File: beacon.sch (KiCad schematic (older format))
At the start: 34 parts

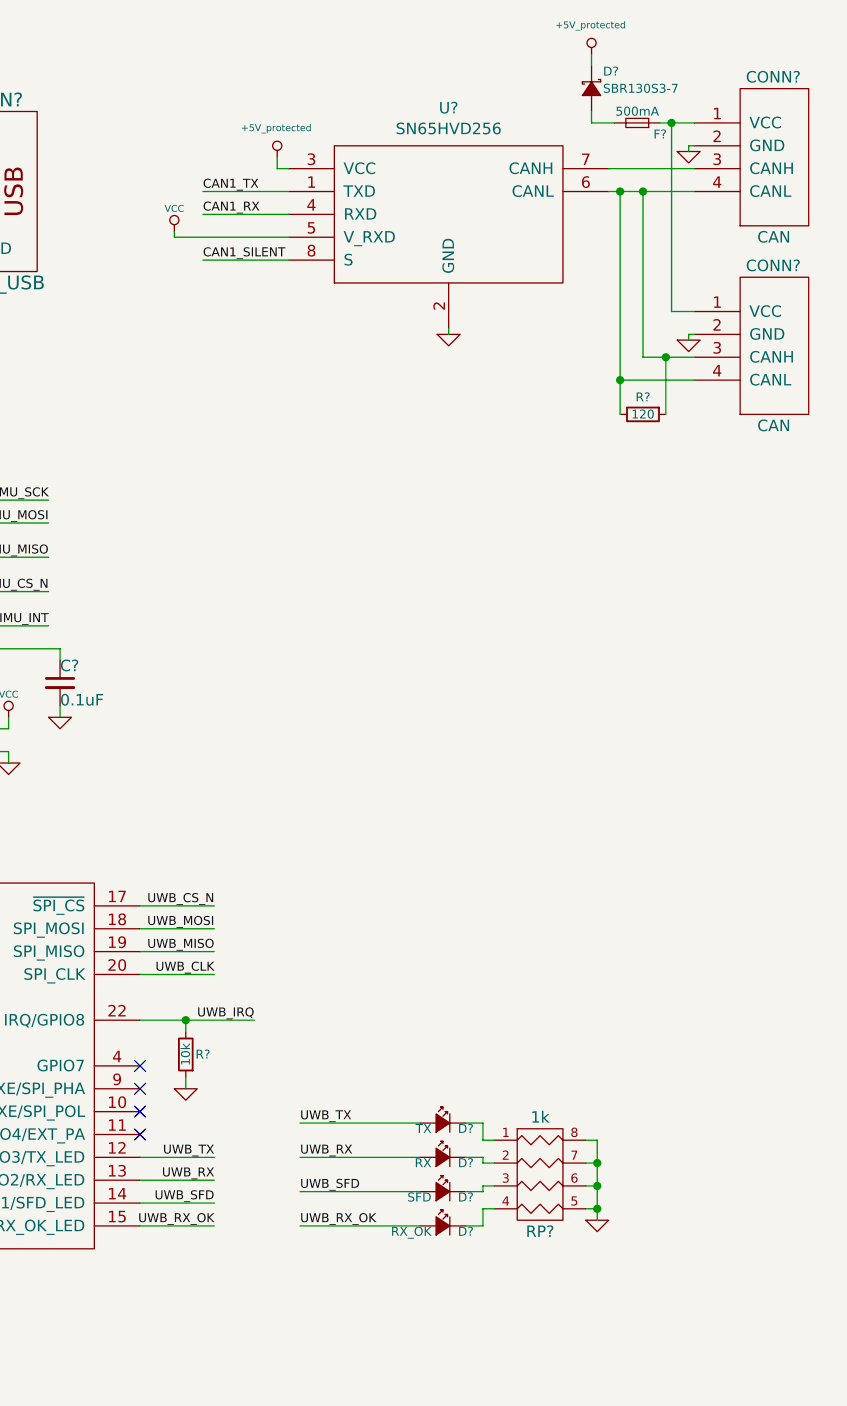
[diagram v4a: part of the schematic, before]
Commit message: Add power regulator for VCC 3.3V
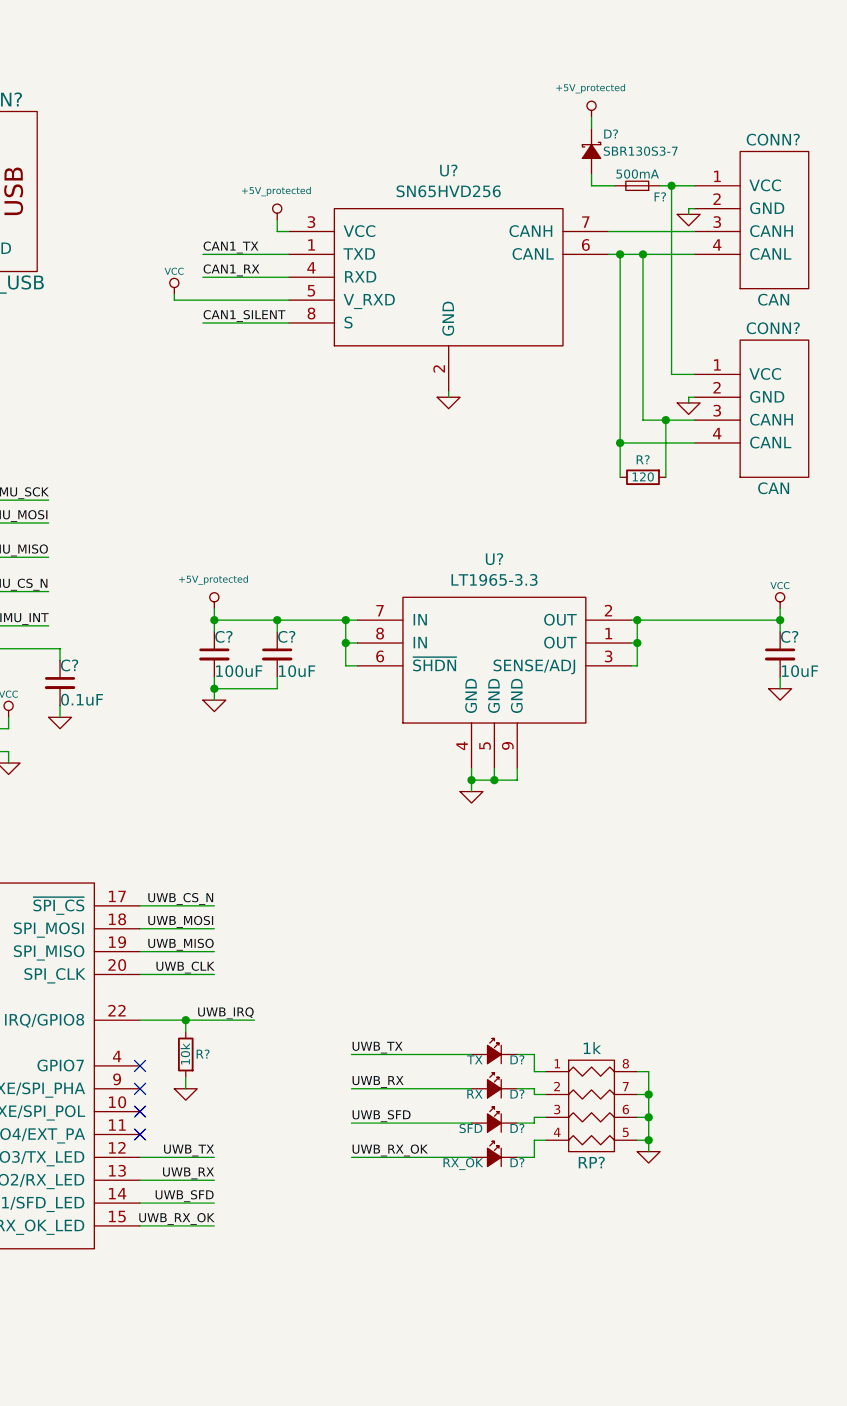
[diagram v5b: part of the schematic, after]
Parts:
- added C? (x2): 10uF, symbol C_Small
- added C?: 100uF, symbol C_Small
- added U?: LT1965-3.3, MODULE, symbol LT1965
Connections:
- net +5V_protected: now also C?.1, C?.1, U?.6 (~SHDN), U?.7 (IN), U?.8 (IN)
- net GND: now also C?.2, C?.2, C?.2, U?.4 (GND), U?.5 (GND), U?.9 (GND)
- net VCC: now also C?.1, U?.1 (OUT), U?.2 (OUT), U?.3 (SENSE/ADJ)
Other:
- moved on the sheet: CONN?, D?, F?, R?, RP?, U?

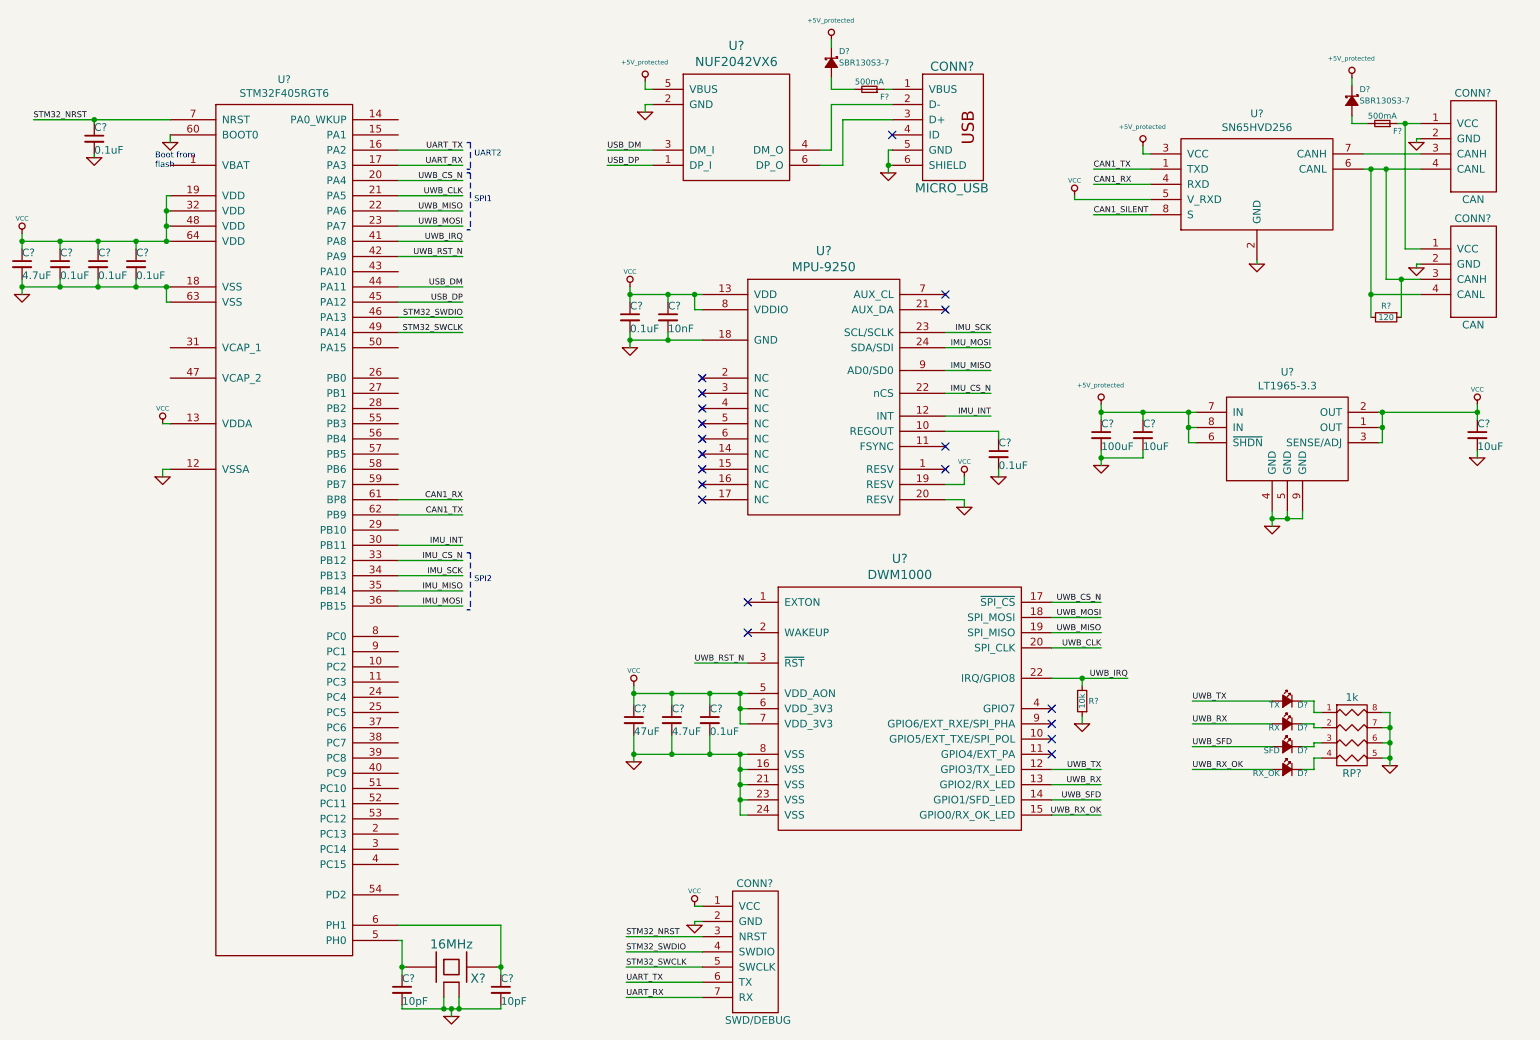
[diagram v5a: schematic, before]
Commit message: Choose an appropriate PTC resettable fuse
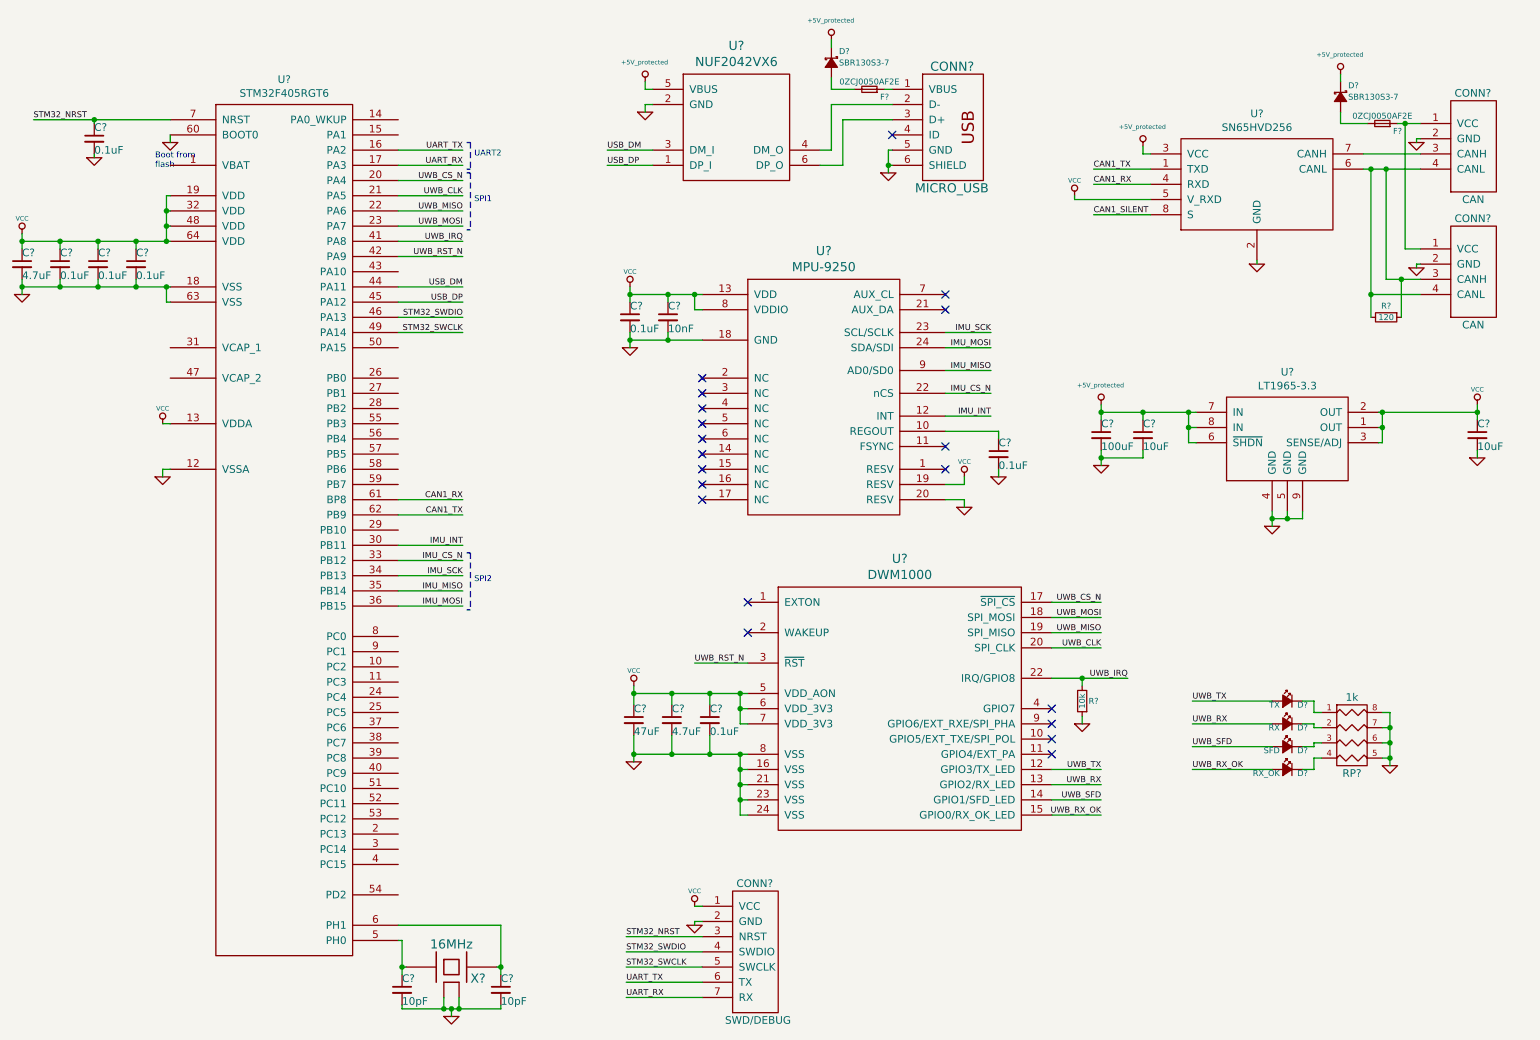
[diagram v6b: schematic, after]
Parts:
- F? (x2): value 500mA -> 0ZCJ0050AF2E
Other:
- moved on the sheet: D?
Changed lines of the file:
@@
 encoding utf-8
 Sheet 1 1
-Title ""
-Date ""
-Rev ""
-Comp ""
+Title "Beacon board"
+Date "2016-06-23"
+Rev "A"
+Comp "CVRA (Club Vaudois de Robotique Autonome)"
 Comment1 ""
 Comment2 ""
@@
 NoConn ~ 7825 5600
 Wire Wire Line
-	1125 1425 2025 1425
+	1125 1425 1525 1425
+Wire Wire Line
+	1525 1425 2025 1425
 Wire Wire Line
 	1525 1425 1525 1450
@@
 Connection ~ 1525 1425
 Wire Wire Line
-	1050 2525 2025 2525
+	1050 2525 1300 2525
+Wire Wire Line
+	1300 2525 1550 2525
+Wire Wire Line
+	1550 2525 1800 2525
+Wire Wire Line
+	1800 2525 2000 2525
+Wire Wire Line
+	2000 2525 2025 2525
 Wire Wire Line
 	2025 2025 2000 2025
 Wire Wire Line
-	2000 2225 2000 1925
+	2000 2225 2000 2125
+Wire Wire Line
+	2000 2125 2000 2025
+Wire Wire Line
+	2000 2025 2000 1925
 Wire Wire Line
 	1975 3425 2025 3425
@@
 	3525 6725 4200 6725
 Wire Wire Line
-	4200 6725 4200 7050
+	4200 6725 4200 7000
+Wire Wire Line
+	4200 7000 4200 7050
 Wire Wire Line
 	4200 7000 4175 7000
 Wire Wire Line
-	3550 6825 3550 7050
+	3550 6825 3550 7000
+Wire Wire Line
+	3550 7000 3550 7050
 Wire Wire Line
 	3550 7000 3575 7000
@@
 	3875 7275 3875 7325
 Wire Wire Line
-	3550 7275 4200 7275
+	3550 7275 3825 7275
+Wire Wire Line
+	3825 7275 3875 7275
+Wire Wire Line
+	3875 7275 3925 7275
+Wire Wire Line
+	3925 7275 4200 7275
 Wire Wire Line
 	3825 7275 3825 7200
@@
 	3525 2525 3950 2525
 Wire Wire Line
-	1050 2225 2025 2225
+	1050 2225 1300 2225
+Wire Wire Line
+	1300 2225 1550 2225
+Wire Wire Line
+	1550 2225 1800 2225
+Wire Wire Line
+	1800 2225 2000 2225
+Wire Wire Line
+	2000 2225 2025 2225
 Wire Wire Line
 	1800 2225 1800 2275
@@
 Connection ~ 1550 2525
 Wire Wire Line
-	1050 2475 1050 2575
+	1050 2475 1050 2525
+Wire Wire Line
+	1050 2525 1050 2575
 Connection ~ 1300 2525
 Connection ~ 1050 2525
@@
 	2000 1925 2025 1925
 Wire Wire Line
-	1050 2175 1050 2275
+	1050 2175 1050 2225
+Wire Wire Line
+	1050 2225 1050 2275
 Wire Wire Line
 	1550 2275 1550 2225
@@
 	5775 5400 5825 5400
 Wire Wire Line
-	5775 5200 5775 5400
+	5775 5200 5775 5300
+Wire Wire Line
+	5775 5300 5775 5400
 Wire Wire Line
 	5575 5200 5575 5275
@@
 Connection ~ 5575 5200
 Wire Wire Line
-	5075 5150 5075 5275
+	5075 5150 5075 5200
+Wire Wire Line
+	5075 5200 5075 5275
 Connection ~ 5325 5200
 Wire Wire Line
@@
 Connection ~ 5775 5300
 Wire Wire Line
-	5075 5600 5825 5600
-Wire Wire Line
-	5775 5600 5775 6000
+	5075 5600 5325 5600
+Wire Wire Line
+	5325 5600 5575 5600
+Wire Wire Line
+	5575 5600 5775 5600
+Wire Wire Line
+	5775 5600 5825 5600
+Wire Wire Line
+	5775 5600 5775 5700
+Wire Wire Line
+	5775 5700 5775 5800
+Wire Wire Line
+	5775 5800 5775 5900
+Wire Wire Line
+	5775 5900 5775 6000
 Wire Wire Line
 	5775 5700 5825 5700
@@
 Connection ~ 5575 5600
 Wire Wire Line
-	5075 5475 5075 5650
+	5075 5475 5075 5600
+Wire Wire Line
+	5075 5600 5075 5650
 Connection ~ 5325 5600
 Connection ~ 5775 5200
 Wire Wire Line
-	5075 5200 5825 5200
+	5075 5200 5325 5200
+Wire Wire Line
+	5325 5200 5575 5200
+Wire Wire Line
+	5575 5200 5775 5200
+Wire Wire Line
+	5775 5200 5825 5200
 Connection ~ 5075 5600
 Connection ~ 5075 5200
@@
 	7825 4900 8150 4900
 Wire Wire Line
-	7825 5100 8325 5100
+	7825 5100 8025 5100
+Wire Wire Line
+	8025 5100 8325 5100
 Wire Wire Line
 	8025 5150 8025 5100
@@
 $EndComp
 Wire Wire Line
-	10050 5325 10050 5675
+	10050 5325 10050 5425
+Wire Wire Line
+	10050 5425 10050 5525
+Wire Wire Line
+	10050 5525 10050 5625
+Wire Wire Line
+	10050 5625 10050 5675
 Wire Wire Line
 	10050 5625 10000 5625
@@
 $EndComp
 Wire Wire Line
-	6750 1625 6750 1775
+	6750 1625 6750 1725
+Wire Wire Line
+	6750 1725 6750 1775
 Wire Wire Line
 	6750 1725 6775 1725
@@
 P 6625 1225
 F 0 "F?" H 6525 1275 39  0000 C CNN
-F 1 "500mA" H 6625 1175 39  0000 C CNN
+F 1 "0ZCJ0050AF2E" H 6625 1175 39  0000 C CNN
 F 2 "" H 6625 1225 50  0000 C CNN
 F 3 "" H 6625 1225 50  0000 C CNN
@@
 	5475 2575 5475 2675
 Wire Wire Line
-	5050 2575 5525 2575
+	5050 2575 5300 2575
+Wire Wire Line
+	5300 2575 5475 2575
+Wire Wire Line
+	5475 2575 5525 2575
 Wire Wire Line
 	5475 2675 5525 2675
@@
 $EndComp
 Wire Wire Line
-	5050 2875 5525 2875
+	5050 2875 5300 2875
+Wire Wire Line
+	5300 2875 5525 2875
 Wire Wire Line
 	5300 2875 5300 2825
 Wire Wire Line
-	5050 2825 5050 2925
+	5050 2825 5050 2875
+Wire Wire Line
+	5050 2875 5050 2925
 Connection ~ 5300 2875
 Wire Wire Line
 	5300 2625 5300 2575
 Wire Wire Line
-	5050 2525 5050 2625
+	5050 2525 5050 2575
+Wire Wire Line
+	5050 2575 5050 2625
 Connection ~ 5300 2575
 Connection ~ 5050 2575
@@
 	9875 1650 10250 1650
 Wire Wire Line
-	9875 1750 10250 1750
-Wire Wire Line
-	9925 1750 9925 2725
+	9875 1750 9925 1750
+Wire Wire Line
+	9925 1750 10025 1750
+Wire Wire Line
+	10025 1750 10250 1750
+Wire Wire Line
+	9925 1750 9925 2575
+Wire Wire Line
+	9925 2575 9925 2725
 Wire Wire Line
 	9925 2575 10250 2575
 Connection ~ 9925 1750
 Wire Wire Line
-	10025 2475 10250 2475
+	10025 2475 10125 2475
+Wire Wire Line
+	10125 2475 10250 2475
 Wire Wire Line
 	10025 2475 10025 1750
@@
 P 10000 1450
 F 0 "F?" H 9900 1500 39  0000 C CNN
-F 1 "500mA" H 10000 1400 39  0000 C CNN
+F 1 "0ZCJ0050AF2E" H 10000 1400 39  0000 C CNN
 F 2 "" H 10000 1450 50  0000 C CNN
 F 3 "" H 10000 1450 50  0000 C CNN
@@
 	10225 1550 10225 1575
 Wire Wire Line
-	10100 1450 10250 1450
+	10100 1450 10150 1450
+Wire Wire Line
+	10150 1450 10250 1450
 Wire Wire Line
 	10150 2275 10150 1450
@@
 L D_Schottky_Small D?
 U 1 1 576C666F
-P 9800 1300
-F 0 "D?" V 9725 1350 39  0000 L CNN
-F 1 "SBR130S3-7" V 9800 1350 39  0000 L CNN
-F 2 "" V 9800 1300 50  0000 C CNN
-F 3 "" V 9800 1300 50  0000 C CNN
-	1    9800 1300
+P 9725 1275
+F 0 "D?" V 9650 1325 39  0000 L CNN
+F 1 "SBR130S3-7" V 9725 1325 39  0000 L CNN
+F 2 "" V 9725 1275 50  0000 C CNN
+F 3 "" V 9725 1275 50  0000 C CNN
+	1    9725 1275
 	0    1    1    0
 $EndComp
 Wire Wire Line
-	9800 1400 9800 1450
-Wire Wire Line
-	9800 1450 9900 1450
+	9725 1375 9725 1450
+Wire Wire Line
+	9725 1450 9900 1450
 $Comp
 L +5V_protected #PWR?
 U 1 1 576C6A7A
-P 9800 1150
-F 0 "#PWR?" H 9800 1240 20  0001 C CNN
-F 1 "+5V_protected" H 9796 1278 30  0000 C CNN
-F 2 "" H 9800 1150 60  0000 C CNN
-F 3 "" H 9800 1150 60  0000 C CNN
-	1    9800 1150
-	1    0    0    -1
-$EndComp
-Wire Wire Line
-	9800 1150 9800 1200
+P 9725 1125
+F 0 "#PWR?" H 9725 1215 20  0001 C CNN
+F 1 "+5V_protected" H 9721 1253 30  0000 C CNN
+F 2 "" H 9725 1125 60  0000 C CNN
+F 3 "" H 9725 1125 60  0000 C CNN
+	1    9725 1125
+	1    0    0    -1
+$EndComp
+Wire Wire Line
+	9725 1125 9725 1175
 $Comp
 L GND #PWR?
@@
 $EndComp
 Wire Wire Line
-	8150 3350 8775 3350
+	8150 3350 8425 3350
+Wire Wire Line
+	8425 3350 8725 3350
+Wire Wire Line
+	8725 3350 8775 3350
 Wire Wire Line
 	8725 3450 8775 3450
 Connection ~ 8725 3350
 Wire Wire Line
-	8725 3350 8725 3550
+	8725 3350 8725 3450
+Wire Wire Line
+	8725 3450 8725 3550
 $Comp
 L C_Small C?
@@
 $EndComp
 Wire Wire Line
-	8150 3300 8150 3400
+	8150 3300 8150 3350
+Wire Wire Line
+	8150 3350 8150 3400
 Wire Wire Line
 	8425 3400 8425 3350
@@
 $EndComp
 Wire Wire Line
-	8150 3600 8150 3700
+	8150 3600 8150 3650
+Wire Wire Line
+	8150 3650 8150 3700
 Wire Wire Line
 	8150 3650 8425 3650
@@
 $EndComp
 Wire Wire Line
-	9275 4000 9275 4100
-Wire Wire Line
-	9275 4050 9475 4050
+	9275 4000 9275 4050
+Wire Wire Line
+	9275 4050 9275 4100
+Wire Wire Line
+	9275 4050 9375 4050
+Wire Wire Line
+	9375 4050 9475 4050
 Wire Wire Line
 	9375 4050 9375 4000
@@
 $EndComp
 Wire Wire Line
-	10625 3300 10625 3400
-Wire Wire Line
-	9975 3350 10625 3350
+	10625 3300 10625 3350
+Wire Wire Line
+	10625 3350 10625 3400
+Wire Wire Line
+	9975 3350 10000 3350
+Wire Wire Line
+	10000 3350 10625 3350
 Connection ~ 10625 3350
 $Comp
@@
 	9975 3450 10000 3450
 Wire Wire Line
-	10000 3350 10000 3550
+	10000 3350 10000 3450
+Wire Wire Line
+	10000 3450 10000 3550
 Connection ~ 10000 3350
 Wire Wire Line
